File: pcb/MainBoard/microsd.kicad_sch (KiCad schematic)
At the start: 14 parts

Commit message: sd card bullshit
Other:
- note added: "active low"
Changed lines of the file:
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@@
+		)
+	)
+	(text "active low"
+		(exclude_from_sim no)
+		(at 46.99 85.598 0)
+		(effects
+			(font
+				(size 1.27 1.27)
+			)
 		)
 	)

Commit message: pcb progress
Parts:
- removed R? (x11): 10k, Resistor_SMD:R_0402_1005Metric, symbol Device:R
- added C202: 22u, Capacitor_SMD:C_0805_2012Metric, symbol Device:C
- added R202, R203, R204, R205, R206, R207, R208, R209, R210, R211, R212: 10k, Resistor_SMD:R_0603_1608Metric, symbol Device:R
- R201: renamed from R?; footprint Resistor_SMD:R_0402_1005Metric -> Resistor_SMD:R_0603_1608Metric; LCSC C25744 -> C25804
- gave numbers to parts that had none: 2
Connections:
- net +3V3: now also C202.1, R202.1, R203.1, R204.1, R205.1, R206.1
- net GND: now also C202.2, R207.2, R208.2, R209.2, R210.2, R211.2, R212.2
- net SD_CS: now also R205.2, R211.1
- net SD_MISO: now also R202.2, R208.1
- net SD_MOSI: now also R204.2, R210.1
- net SD_SCLK: now also R203.2, R209.1
- net SD_DAT1: now reaches R201.2, U201.8 (DAT1)
- net SD_DAT1: now also R207.1
- net SD_DAT2: now reaches U201.1 (DAT2)
- net SD_DAT2: now also R206.2, R212.1

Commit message: dump pcb
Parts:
- added R213, R214, R215, R216: 47k, Resistor_SMD:R_0603_1608Metric, symbol Device:R
- R201, R202, R204, R205, R206, R211, R212: value 10k -> 47k; LCSC C25804 -> (none)
- R203: value 10k -> 47k; LCSC C25804 -> (none); now not fitted; now left out of the parts list
- R207, R208, R209, R210: value 10k -> 33R; footprint Resistor_SMD:R_0603_1608Metric -> Resistor_SMD:R_0402_1005Metric; LCSC C25804 -> C25105; now fitted; now in the parts list
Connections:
- net GND: now also R213.2, R214.2, R215.2, R216.2; no longer R207.2, R208.2, R209.2, R210.2
- net SD_CS: now also R207.1; no longer R205.2, R211.1, U201.2 (DAT3/CD)
- net SD_DAT1: now also R211.1; no longer R207.1
- net SD_DAT2: now also R216.1; no longer R212.1
- net SD_MISO: now also R210.1; no longer R202.2, R208.1, U201.7 (DAT0)
- net SD_MOSI: now also R208.1; no longer R204.2, R210.1, U201.3 (CMD)
- net SD_SCLK: no longer R203.2, U201.5 (CLK)
- new net SD_CLK: R203.2, R209.2, R213.1, U201.5 (CLK)
- new net SD_CS_DAT3: R205.2, R207.2, R215.1, U201.2 (DAT3/CD)
- new net SD_MISO_DAT0: R202.2, R210.2, R212.1, U201.7 (DAT0)
- new net SD_MOSI_CMD: R204.2, R208.2, R214.1, U201.3 (CMD)
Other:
- note added: "MISO at sd card, others at rp2040"

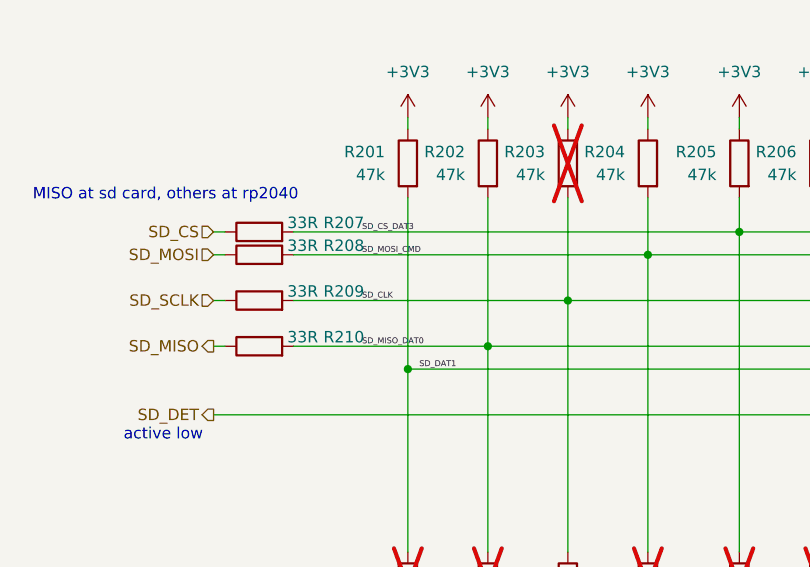
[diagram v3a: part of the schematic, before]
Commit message: MainBoard: fixes, simplify, BOM optimize, DRC fixes, ERC fixes
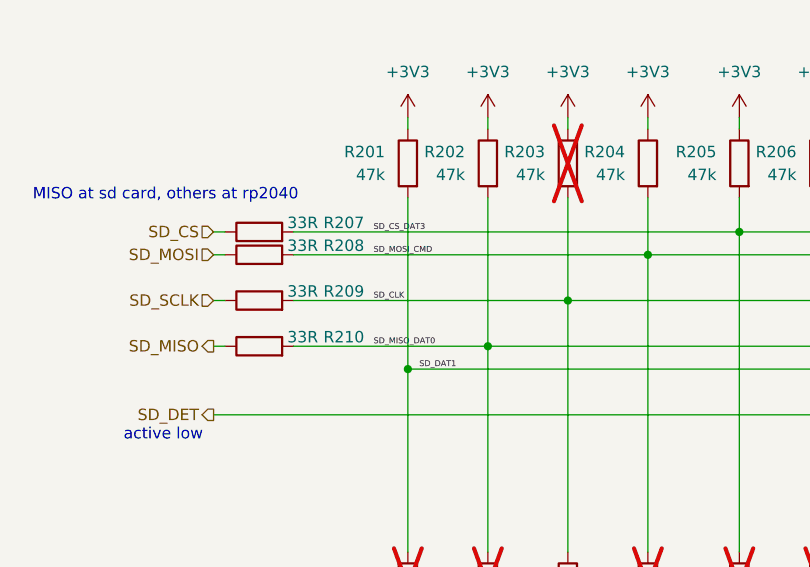
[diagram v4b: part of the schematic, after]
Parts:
- C201: LCSC C307331 -> C1525
- R201, R202, R203, R204, R205, R206, R211, R212, R213, R214, R215, R216: LCSC (none) -> C25819
- U201: now left out of the parts list
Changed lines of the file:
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@@
+	(wire
+		(pts
+			(xy 52.07 69.85) (xy 82.55 69.85)
+		)
+		(stroke
+			(width 0)
+			(type default)
+		)
+	)
+	(wire
+		(pts
+			(xy 82.55 69.85) (xy 82.55 97.79)
+		)
+		(stroke
+			(width 0)
+			(type default)
+		)
+	)
+	(wire
+		(pts
+			(xy 101.6 58.42) (xy 101.6 62.23)
+		)
+		(stroke
+			(width 0)
+			(type default)
+		)
+	)
+	(wire
+		(pts
+			(xy 110.49 97.79) (xy 110.49 59.69)
+		)
+		(stroke
+			(width 0)
+			(type default)
+		)
+	)
+	(wire
+		(pts
+			(xy 52.07 64.77) (xy 91.44 64.77)
+		)
+		(stroke
+			(width 0)
+			(type default)
+		)
+	)
+	(wire
+		(pts
+			(xy 152.4 92.71) (xy 153.67 92.71)
+		)
+		(stroke
+			(width 0)
+			(type default)
+		)
+	)
+	(wire
+		(pts
+			(xy 44.45 62.23) (xy 43.18 62.23)
+		)
+		(stroke
+			(width 0)
+			(type default)
+		)
+	)
 	(wire
 		(pts
@@
 	(wire
 		(pts
-			(xy 82.55 69.85) (xy 82.55 97.79)
-		)
-		(stroke
-			(width 0)
-			(type default)
-		)
-	)
-	(wire
-		(pts
-			(xy 101.6 58.42) (xy 101.6 62.23)
-		)
-		(stroke
-			(width 0)
-			(type default)
-		)
-	)
-	(wire
-		(pts
-			(xy 110.49 97.79) (xy 110.49 59.69)
-		)
-		(stroke
-			(width 0)
-			(type default)
-		)
-	)
-	(wire
-		(pts
-			(xy 152.4 92.71) (xy 153.67 92.71)
-		)
-		(stroke
-			(width 0)
-			(type default)
-		)
-	)
-	(wire
-		(pts
-			(xy 44.45 62.23) (xy 43.18 62.23)
-		)
-		(stroke
-			(width 0)
-			(type default)
-		)
-	)
-	(wire
-		(pts
-			(xy 52.07 64.77) (xy 91.44 64.77)
-		)
-		(stroke
-			(width 0)
-			(type default)
-		)
-	)
-	(wire
-		(pts
 			(xy 116.84 67.31) (xy 116.84 36.83)
 		)
@@
 		(pts
 			(xy 124.46 36.83) (xy 137.16 36.83)
-		)
-		(stroke
-			(width 0)
-			(type default)
-		)
-	)
-	(wire
-		(pts
-			(xy 52.07 69.85) (xy 82.55 69.85)
 		)
 		(stroke
@@
 	)
 	(label "SD_CLK"
-		(at 59.69 69.85 0)
+		(at 60.96 69.85 0)
 		(fields_autoplaced yes)
 		(effects
@@
 	)
 	(label "SD_CS_DAT3"
-		(at 59.69 62.23 0)
+		(at 60.96 62.23 0)
 		(fields_autoplaced yes)
 		(effects
@@
 	)
 	(label "SD_MOSI_CMD"
-		(at 59.69 64.77 0)
+		(at 60.96 64.77 0)
 		(fields_autoplaced yes)
 		(effects
@@
 	)
 	(label "SD_MISO_DAT0"
-		(at 59.69 74.93 0)
+		(at 60.96 74.93 0)
 		(fields_autoplaced yes)
 		(effects
@@
 			)
 		)
-		(property "LCSC" ""
+		(property "LCSC" "C25819"
 			(at 91.44 101.6 0)
 			(effects
@@
 			)
 		)
-		(property "LCSC" ""
+		(property "LCSC" "C25819"
 			(at 110.49 54.61 0)
 			(effects
@@
 			)
 		)
-		(property "LCSC" ""
+		(property "LCSC" "C25819"
 			(at 73.66 54.61 0)
 			(effects
@@
 			)
 		)
-		(property "LCSC" ""
+		(property "LCSC" "C25819"
 			(at 73.66 101.6 0)
 			(effects
@@
 			)
 		)
-		(property "LCSC" ""
+		(property "LCSC" "C25819"
 			(at 110.49 101.6 0)
 			(effects
@@
 			)
 		)
-		(property "LCSC" ""
+		(property "LCSC" "C25819"
 			(at 64.77 54.61 0)
 			(effects
@@
 			)
 		)
-		(property "LCSC" ""
+		(property "LCSC" "C25819"
 			(at 91.44 54.61 0)
 			(effects
@@
 		(unit 1)
 		(exclude_from_sim no)
-		(in_bom yes)
+		(in_bom no)
 		(on_board yes)
 		(dnp no)
@@
 			)
 		)
-		(property "LCSC" ""
+		(property "LCSC" "C25819"
 			(at 101.6 54.61 0)
 			(effects
@@
 			)
 		)
-		(property "LCSC" ""
+		(property "LCSC" "C25819"
 			(at 82.55 101.6 0)
 			(effects
@@
 			)
 		)
-		(property "LCSC" "C307331"
+		(property "LCSC" "C1525"
 			(at 124.46 40.64 0)
 			(effects
@@
 			)
 		)
-		(property "LCSC" ""
+		(property "LCSC" "C25819"
 			(at 64.77 101.6 0)
 			(effects
@@
 			)
 		)
-		(property "LCSC" ""
+		(property "LCSC" "C25819"
 			(at 101.6 101.6 0)
 			(effects
@@
 			)
 		)
-		(property "LCSC" ""
+		(property "LCSC" "C25819"
 			(at 82.55 54.61 0)
 			(effects

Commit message: pcb: fixes, improvements
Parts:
- R201, R202, R203, R204, R205, R206, R211, R212, R213, R214, R215, R216: value 47k -> 10k; LCSC C25819 -> C25804
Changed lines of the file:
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@@
 			)
 		)
-		(property "Value" "47k"
+		(property "Value" "10k"
 			(at 88.9 102.8699 0)
 			(effects
@@
 			)
 		)
-		(property "LCSC" "C25819"
+		(property "LCSC" "C25804"
 			(at 91.44 101.6 0)
 			(effects
@@
 			)
 		)
-		(property "Value" "47k"
+		(property "Value" "10k"
 			(at 107.95 55.8799 0)
 			(effects
@@
 			)
 		)
-		(property "LCSC" "C25819"
+		(property "LCSC" "C25804"
 			(at 110.49 54.61 0)
 			(effects
@@
 			)
 		)
-		(property "Value" "47k"
+		(property "Value" "10k"
 			(at 71.12 55.8799 0)
 			(effects
@@
 			)
 		)
-		(property "LCSC" "C25819"
+		(property "LCSC" "C25804"
 			(at 73.66 54.61 0)
 			(effects
@@
 			)
 		)
-		(property "Value" "47k"
+		(property "Value" "10k"
 			(at 71.12 102.8699 0)
 			(effects
@@
 			)
 		)
-		(property "LCSC" "C25819"
+		(property "LCSC" "C25804"
 			(at 73.66 101.6 0)
 			(effects
@@
 			)
 		)
-		(property "Value" "47k"
+		(property "Value" "10k"
 			(at 107.95 102.8699 0)
 			(effects
@@
 			)
 		)
-		(property "LCSC" "C25819"
+		(property "LCSC" "C25804"
 			(at 110.49 101.6 0)
 			(effects
@@
 			)
 		)
-		(property "Value" "47k"
+		(property "Value" "10k"
 			(at 62.23 55.8799 0)
 			(effects
@@
 			)
 		)
-		(property "LCSC" "C25819"
+		(property "LCSC" "C25804"
 			(at 64.77 54.61 0)
 			(effects
@@
 			)
 		)
-		(property "Value" "47k"
+		(property "Value" "10k"
 			(at 88.9 55.8799 0)
 			(effects
@@
 			)
 		)
-		(property "LCSC" "C25819"
+		(property "LCSC" "C25804"
 			(at 91.44 54.61 0)
 			(effects
@@
 			)
 		)
-		(property "Value" "47k"
+		(property "Value" "10k"
 			(at 99.06 55.8799 0)
 			(effects
@@
 			)
 		)
-		(property "LCSC" "C25819"
+		(property "LCSC" "C25804"
 			(at 101.6 54.61 0)
 			(effects
@@
 			)
 		)
-		(property "Value" "47k"
+		(property "Value" "10k"
 			(at 80.01 102.8699 0)
 			(effects
@@
 			)
 		)
-		(property "LCSC" "C25819"
+		(property "LCSC" "C25804"
 			(at 82.55 101.6 0)
 			(effects
@@
 			)
 		)
-		(property "Value" "47k"
+		(property "Value" "10k"
 			(at 62.23 102.8699 0)
 			(effects
@@
 			)
 		)
-		(property "LCSC" "C25819"
+		(property "LCSC" "C25804"
 			(at 64.77 101.6 0)
 			(effects
@@
 			)
 		)
-		(property "Value" "47k"
+		(property "Value" "10k"
 			(at 99.06 102.8699 0)
 			(effects
@@
 			)
 		)
-		(property "LCSC" "C25819"
+		(property "LCSC" "C25804"
 			(at 101.6 101.6 0)
 			(effects
@@
 			)
 		)
-		(property "Value" "47k"
+		(property "Value" "10k"
 			(at 80.01 55.8799 0)
 			(effects
@@
 			)
 		)
-		(property "LCSC" "C25819"
+		(property "LCSC" "C25804"
 			(at 82.55 54.61 0)
 			(effects
